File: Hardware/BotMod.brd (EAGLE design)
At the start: 80 x 31 mm, 39 parts, among them Q1 BSS138, Q2 BSS138, T1 MMBT2222A, U1 LSM303D

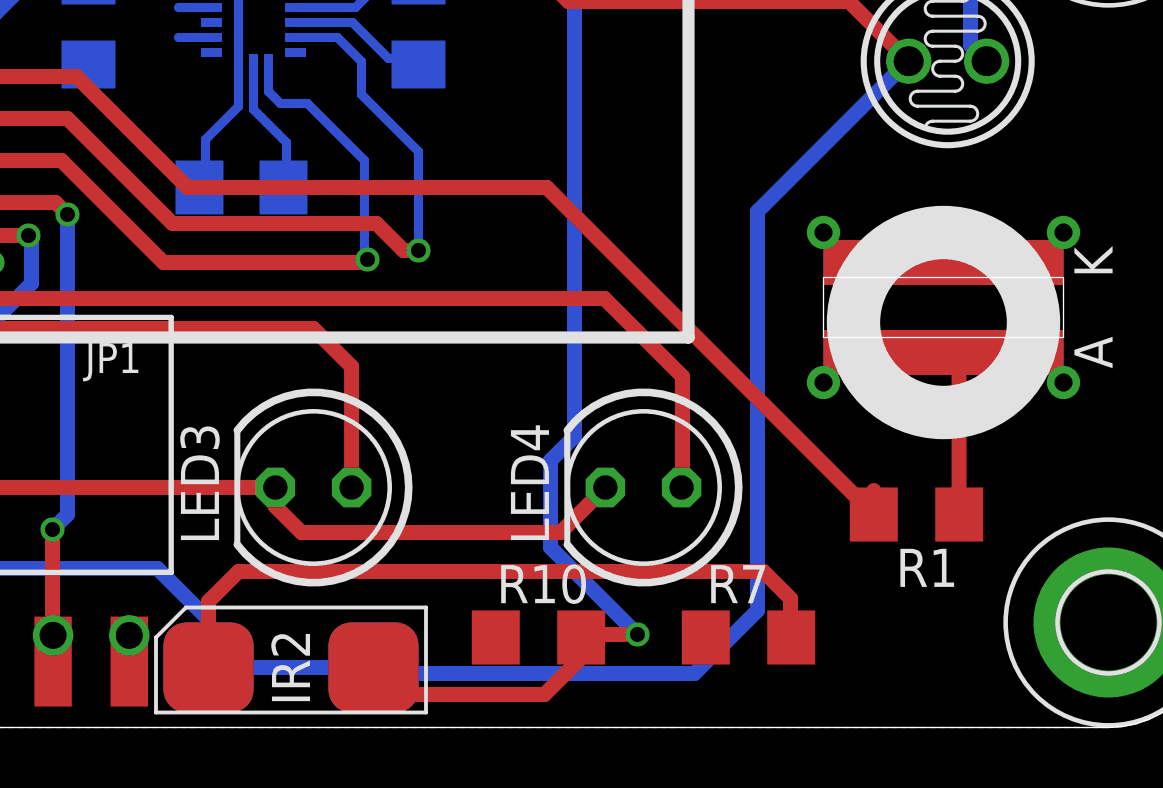
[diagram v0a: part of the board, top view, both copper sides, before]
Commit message: Laser resistor removed
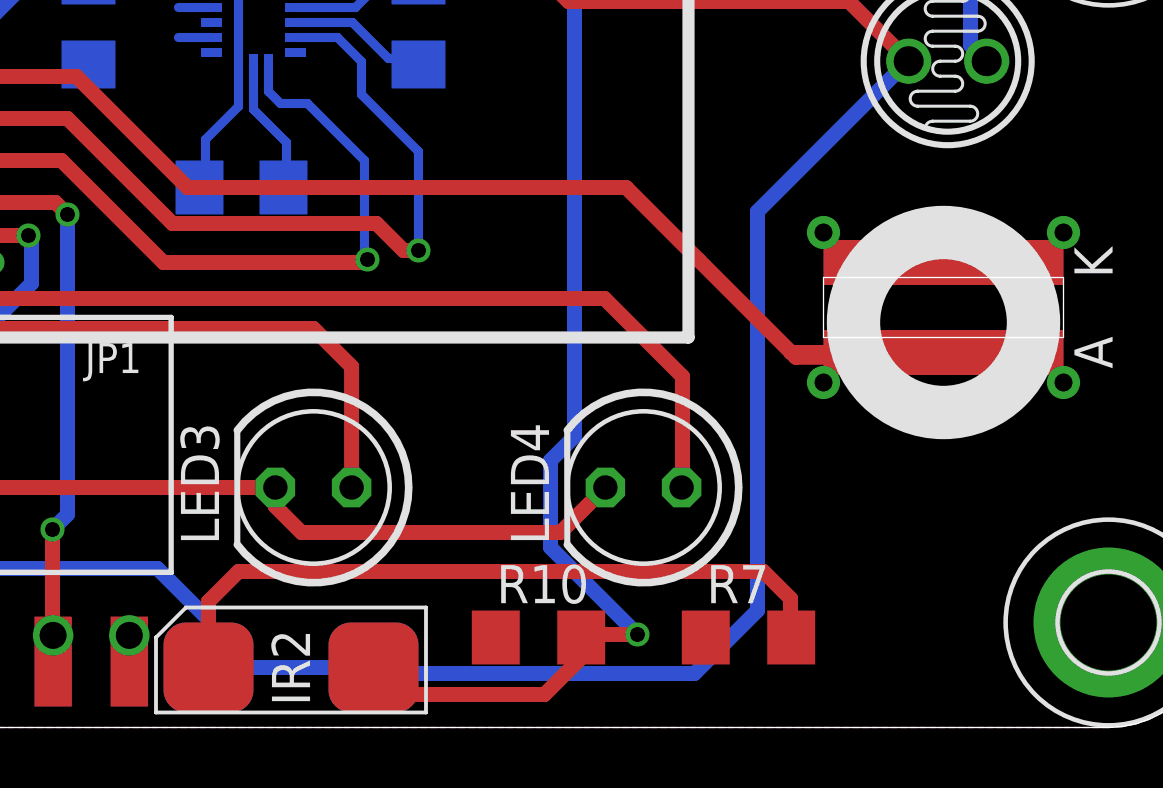
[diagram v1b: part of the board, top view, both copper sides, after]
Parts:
- removed R1: 90, resistor:R1206
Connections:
- removed net N$9: LD.A, LD.A1, R1.1
- net D5: now also LD.A, LD.A1; no longer R1.2
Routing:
- net D5: track 44.9 -> 53.8 mm
- net N$9: track 5.62 -> 0.00 mm
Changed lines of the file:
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@@
 <element name="R8" library="resistor" package="R1206" value="1k" x="4.5" y="17.7" rot="R90"/>
 <element name="LD" library="SpaceDIY" package="KEYES_LASER" value="LASER" x="71" y="14" rot="R270"/>
-<element name="R1" library="resistor" package="R1206" value="90" x="70.1" y="7.1" rot="R180"/>
 <element name="U1" library="LSM303D" package="LGA3X3_16L" value="LSM303D" x="48" y="23.5" rot="MR0"/>
 <element name="C1" library="resistor" package="C1206" value="0.1uF" x="42.5" y="23.5" rot="MR270"/>
@@
 <signal name="D5">
 <contactref element="SV1" pad="9"/>
-<contactref element="R1" pad="2"/>
 <wire x1="32.54" y1="23.73" x2="32.54" y2="21.96" width="0.5" layer="1"/>
 <wire x1="32.54" y1="21.96" x2="32.8" y2="21.7" width="0.5" layer="1"/>
-<wire x1="68.678" y1="7.1" x2="68.678" y2="7.9" width="0.5" layer="1"/>
 <wire x1="32.8" y1="21.7" x2="42.1" y2="21.7" width="0.5" layer="1"/>
 <wire x1="42.1" y1="21.7" x2="45.8" y2="18" width="0.5" layer="1"/>
-<wire x1="45.8" y1="18" x2="57.778" y2="18" width="0.5" layer="1"/>
-<wire x1="57.778" y1="18" x2="68.678" y2="7.1" width="0.5" layer="1"/>
+<wire x1="45.8" y1="18" x2="60.42" y2="18" width="0.5" layer="1"/>
+<contactref element="LD" pad="A"/>
+<contactref element="LD" pad="A1"/>
+<wire x1="60.42" y1="18" x2="62.85" y2="15.57" width="0.5" layer="1"/>
+<wire x1="65.92" y1="12.5" x2="66.08" y2="12.34" width="0.5" layer="1"/>
+<wire x1="66.08" y1="12.34" x2="67.16" y2="12.34" width="0.5" layer="1"/>
+<wire x1="67.16" y1="12.34" x2="70.51" y2="12.34" width="0.5" layer="1"/>
+<wire x1="70.51" y1="12.34" x2="70.84" y2="12.34" width="0.5" layer="1"/>
+<wire x1="70.84" y1="12.34" x2="71" y2="12.5" width="0.5" layer="1"/>
+<wire x1="71" y1="12.5" x2="70.67" y2="12.5" width="0.5" layer="1"/>
+<wire x1="70.67" y1="12.5" x2="70.51" y2="12.34" width="0.5" layer="1"/>
+<wire x1="71" y1="12.5" x2="67.32" y2="12.5" width="0.5" layer="1"/>
+<wire x1="67.32" y1="12.5" x2="67.16" y2="12.34" width="0.5" layer="1"/>
+<wire x1="71" y1="12.5" x2="65.92" y2="12.5" width="0.5" layer="1"/>
+<wire x1="65.92" y1="12.5" x2="62.85" y2="15.57" width="0.5" layer="1"/>
+<wire x1="71" y1="12.5" x2="71" y2="12.5" width="0" layer="19" extent="1-16"/>
 </signal>
 <signal name="D6">
@@
 <wire x1="12.228" y1="16.278" x2="12.65" y2="16.7" width="0.5" layer="1"/>
 </signal>
-<signal name="N$9">
-<contactref element="LD" pad="A1"/>
-<contactref element="LD" pad="A"/>
-<contactref element="R1" pad="1"/>
-<wire x1="71.522" y1="7.1" x2="71.522" y2="11.978" width="0.5" layer="1"/>
-<wire x1="71.522" y1="11.978" x2="71" y2="12.5" width="0.5" layer="1"/>
-<wire x1="71" y1="12.5" x2="71" y2="12.5" width="0" layer="19" extent="1-16"/>
-</signal>
 <signal name="N$10">

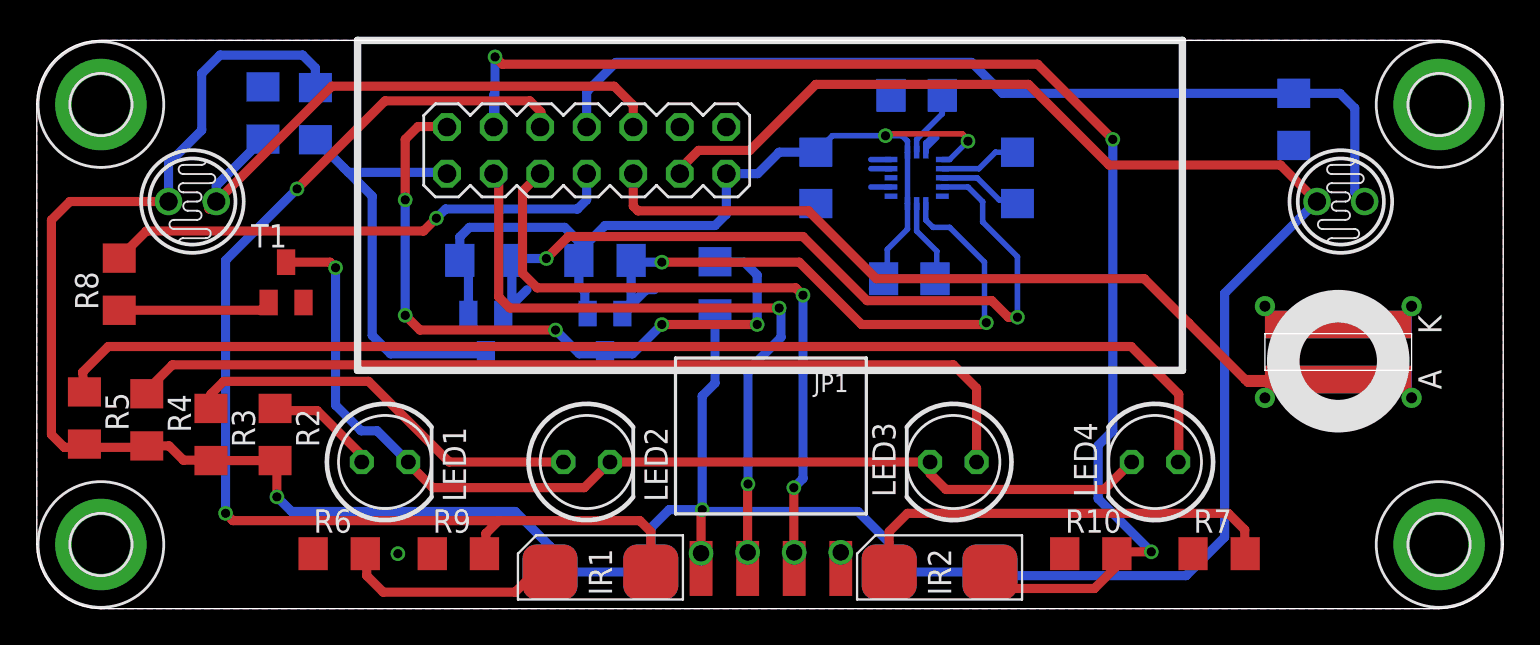
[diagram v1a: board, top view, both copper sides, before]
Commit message: Mod connector updated to 16 pin
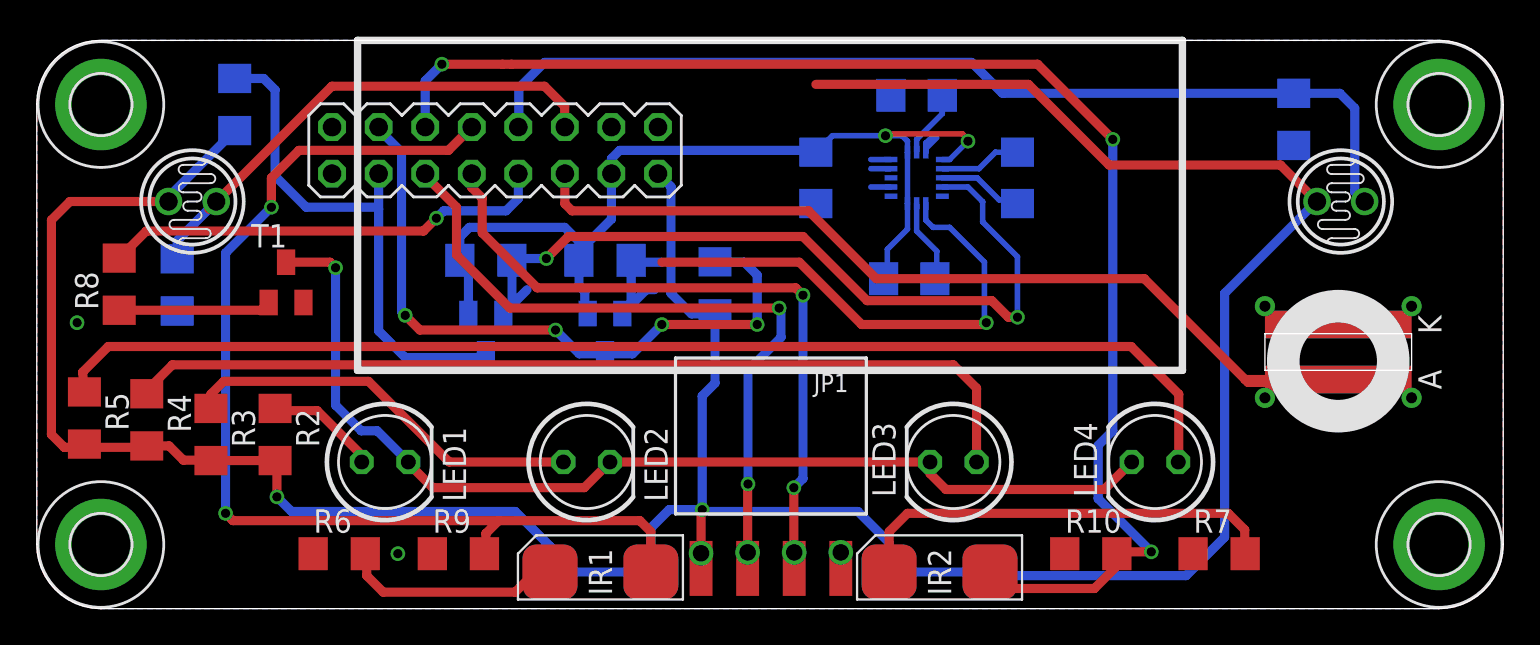
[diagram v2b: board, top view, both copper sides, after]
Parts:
- removed SV1: Mods, con-lstb:MA07-2
- added SV2: (no value), con-lstb:MA08-2
- moved R11 10.5 mm to (7.66, 17.7), turned to 90 degrees
- moved R16 4.43 mm to (10.8, 27.5), turned to 270 degrees
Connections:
- net 3.3V: now also SV2.13; no longer SV1.13
- net A1: now also SV2.12; no longer SV1.10
- net A2: now also SV2.10; no longer SV1.8
- net A3: now also SV2.8; no longer SV1.6
- net A4: now also SV2.6; no longer SV1.4
- net D2: now also SV2.4; no longer SV1.2
- net D3: now also SV2.3; no longer SV1.1
- net D5: now also SV2.11; no longer SV1.9
- net D6: now also SV2.9; no longer SV1.7
- net D7: now also SV2.7; no longer SV1.5
- net D8: now also SV2.5; no longer SV1.3
- net GND: now also SV2.14, SV2.16; no longer SV1.12
- net VCC: now also SV2.15; no longer SV1.11
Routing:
- net VCC: track 184.0 -> 173.7 mm
- net D3: track 24.0 -> 28.7 mm
- net A3: track 63.6 -> 59.3 mm
- net A1: track 32.6 -> 28.3 mm
- net A2: track 50.8 -> 54.7 mm
- net D6: track 28.2 -> 24.5 mm
- net D5: track 53.8 -> 57.5 mm
- net D8: track 37.4 -> 38.9 mm
- net D2: track 38.2 -> 36.9 mm, vias 5 -> 4
- net A4: track 75.6 -> 76.5 mm
- net D7: track 36.7 -> 37.5 mm
- net 3.3V: track 52.1 -> 52.8 mm
- net SDA: vias 2 -> 1
- net GND: vias 1 -> 2

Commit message: SCH and BRD updated Production Files (GERBER, BOM and Centroid)
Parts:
- removed R16: 10k, resistor:R1206
- added R1: 200, resistor:R1206
- R7: value 200 -> 1k
- R8: value 1k -> 10k
- moved R7 61.8 mm to (4.50, 17.7), turned to 90 degrees
- moved R8 11.7 mm to (10.8, 27.5), flipped to the bottom, turned to 270 degrees
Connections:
- net D3: now also R8.1; no longer R16.1
- net D6: now also R7.2; no longer R8.2
- net GND: now also R1.1; no longer R7.1
- net N$2: now also R7.1; no longer R8.1
- net N$4: now also R1.2; no longer R7.2
- net VCC: now also R8.2; no longer R16.2
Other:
- board text added: "U1"

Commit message: Update gerber for production
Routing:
- net SDA: track 34.6 -> 32.4 mm, vias 1 -> 2
- net SCL: track 44.5 -> 42.7 mm

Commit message: Update
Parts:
- added JP2, JP3: (no value), pinhead:1X03
- added S1: (no value), bt_electromech:DPDT_JS202011CQN
- moved LD 1.40 mm to (69.6, 14.0), turned to 90 degrees
- moved R1 1.20 mm to (63.3, 3.00)
- moved R10 0.80 mm to (56.7, 3.00)
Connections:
- new net LAS: LD.A, LD.A1, S1.4
- new net LED: R7.2, S1.1
- new net S1: JP2.1, S1.3
- new net S2: JP3.1, S1.6
- net D5: now also S1.5; no longer LD.A, LD.A1
- net D6: now also S1.2; no longer R7.2
- net GND: now also JP2.3, JP3.3
- net VCC: now also JP2.2, JP3.2
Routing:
- net LED: track 0.00 -> 90.5 mm
- net S1: track 0.00 -> 78.5 mm
- net D6: track 24.5 -> 65.4 mm
- net VCC: track 173.7 -> 160.7 mm, vias 3 -> 4
- net S2: track 0.00 -> 10.9 mm
- net LAS: track 0.00 -> 6.42 mm
- net A4: track 76.5 -> 74.7 mm
- net D5: track 57.5 -> 58.8 mm
- net N$1: track 57.9 -> 58.9 mm, vias 1 -> 3
- net N$4: track 23.7 -> 22.8 mm
- net GND: vias 2 -> 4
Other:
- board text added: "LED/LASER"
- board text added: "SERVOS"

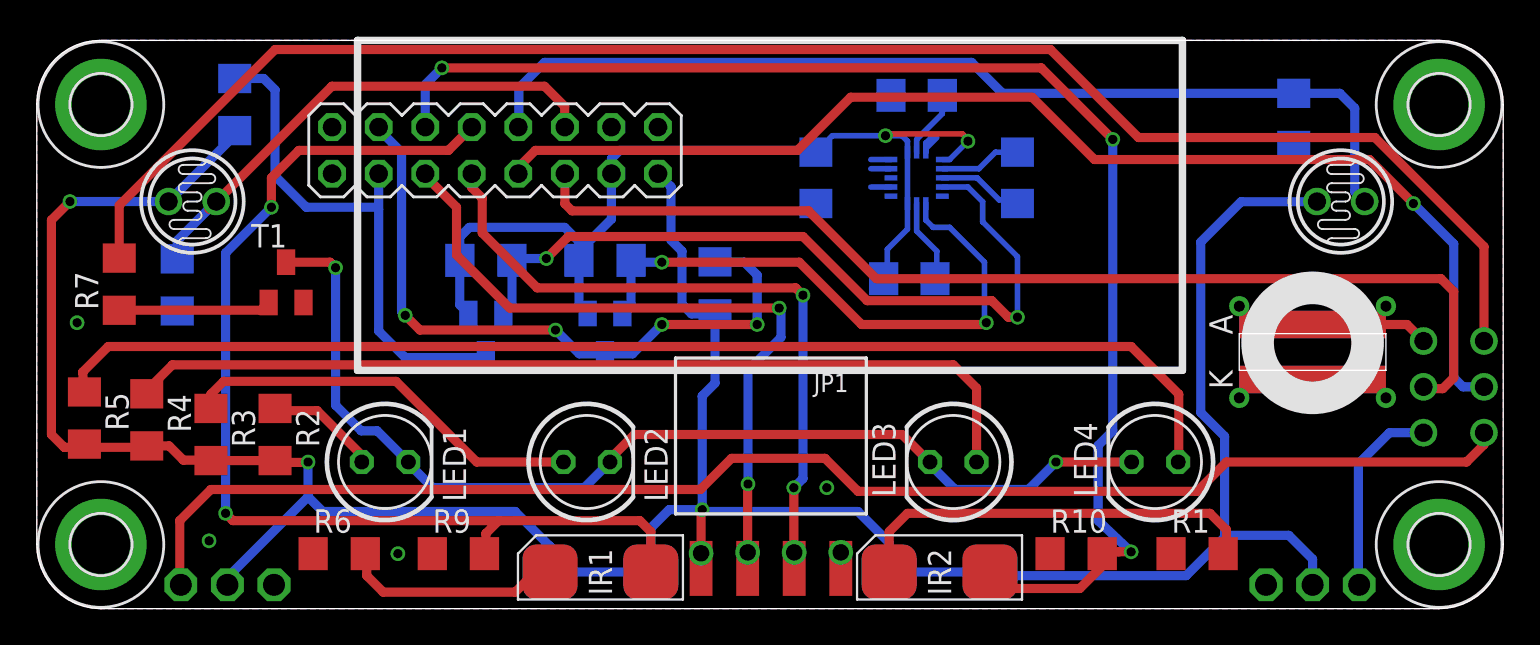
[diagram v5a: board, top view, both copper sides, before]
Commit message: Updated design files: - Added support for GPS through Serial port - Silkscreen layouts improved
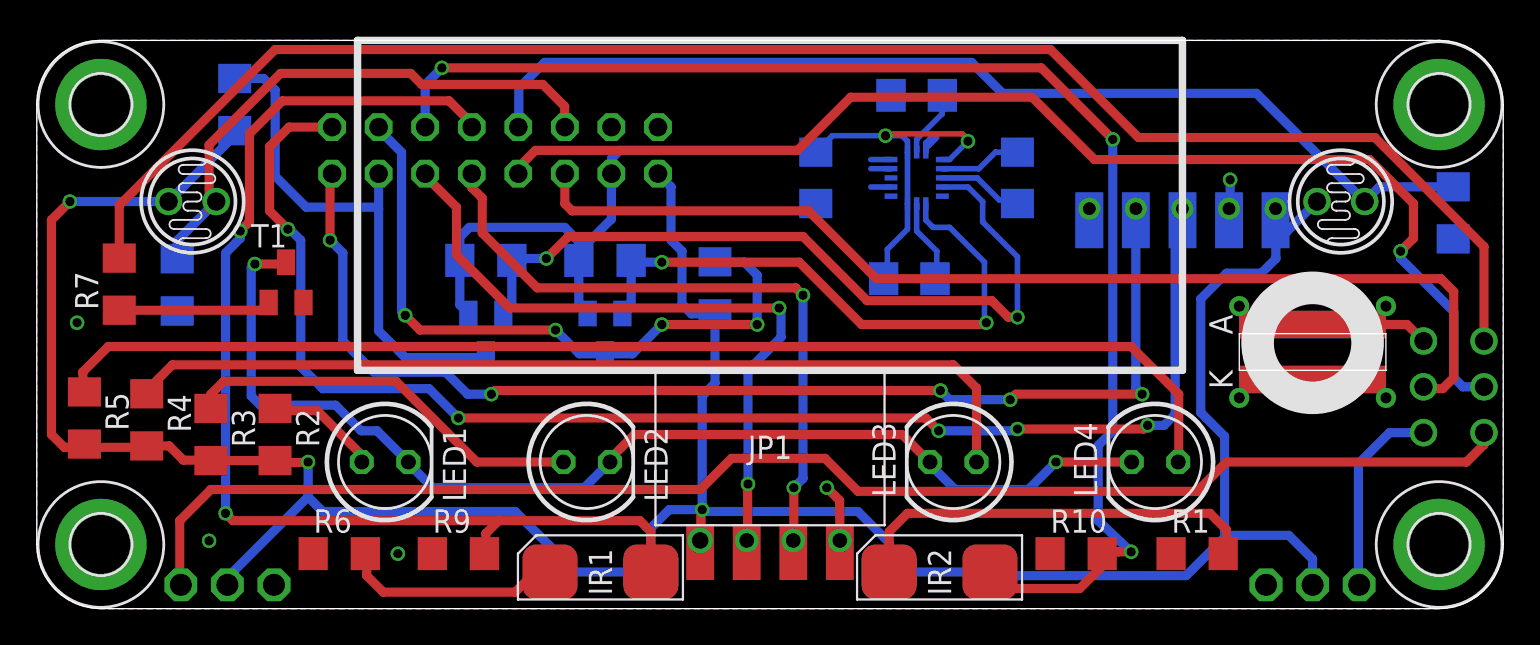
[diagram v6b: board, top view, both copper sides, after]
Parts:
- added JP4: (no value), pinhead:1X03
- JP1: device SparkFun-Connectors:1X04_SMD_RA_FEMALE -> SpaceDIY_connectors:PINHEAD_4_FEMALE
- JP2: device pinhead:1X03 -> SpaceDIY_connectors:PINHEAD_5_FEMALE
- moved JP2 58.0 mm to (62.5, 26.9), turned to 0 degrees
- moved R12 10.1 mm to (77.3, 21.6)
- moved JP1 0.62 mm to (40.0, 8.80), turned to 0 degrees
- flipped SV1 to the bottom, turned to 180 degrees
- renumbered SV2 to SV1
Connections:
- new net D0: JP2.P$3, SV1.1
- new net D1: JP2.P$4, SV1.2
- net 3.3V: now also SV1.14; no longer SV1.13
- net A1: now also SV1.11; no longer SV1.12
- net A2: now also SV1.9; no longer SV1.10
- net A3: now also SV1.7; no longer SV1.8
- net A4: now also SV1.5; no longer SV1.6
- net D2: now also SV1.3; no longer SV1.4
- net D3: now also SV1.4; no longer SV1.3
- net D5: now also SV1.12; no longer SV1.11
- net D6: now also SV1.10; no longer SV1.9
- net D7: now also JP1.P$3, SV1.8; no longer JP1.2, SV1.7
- net D8: now also JP1.P$2, SV1.6; no longer JP1.3, SV1.5
- net GND: now also JP1.P$4, JP2.P$2, JP4.3, SV1.13, SV1.15; no longer JP1.1, JP2.3, SV1.14, SV1.16
- net S1: now also JP4.1; no longer JP2.1
- net VCC: now also JP1.P$1, JP2.P$1, JP4.2, SV1.16; no longer JP1.4, JP2.2, SV1.15
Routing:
- net D0: track 0.00 -> 77.4 mm, vias 0 -> 5
- net D1: track 0.00 -> 64.9 mm, vias 0 -> 5
- net GND: track 9.99 -> 18.4 mm, vias 4 -> 5
- net N$1: track 58.9 -> 62.4 mm
- net A3: track 59.3 -> 62.8 mm
- net A2: track 54.7 -> 57.7 mm
- net A1: track 28.3 -> 31.0 mm
- net VCC: track 160.7 -> 162.7 mm, vias 4 -> 3
- net D8: track 38.9 -> 40.1 mm, vias 3 -> 2
- net D7: track 37.5 -> 38.4 mm
- net D6: track 65.4 -> 66.0 mm
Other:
- board text added: "+"
- board text added: "-"
- board text added: "GPS"
- board text added: "S"
